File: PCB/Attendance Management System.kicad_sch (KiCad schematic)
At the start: 0 parts

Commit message: Power schematic is ready
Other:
- added sheet MCU (mcu.kicad_sch)
- added sheet Power (power.kicad_sch)
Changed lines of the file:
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@@
 	(generator_version "10.0")
 	(paper "A4")
+	(sheet
+		(at 120.65 83.185)
+		(size 46.99 44.45)
+		(exclude_from_sim no)
+		(in_bom yes)
+		(on_board yes)
+		(dnp no)
+		(fields_autoplaced yes)
+		(stroke
+			(width 0.1524)
+			(type solid)
+		)
+		(fill
+			(color 0 0 0 0)
+		)
+		(property "Sheetname" "MCU"
+			(at 120.65 82.4734 0)
+			(show_name no)
+			(do_not_autoplace no)
+			(effects
+				(font
+					(size 1.27 1.27)
+				)
+				(justify left bottom)
+			)
+		)
+		(property "Sheetfile" "mcu.kicad_sch"
+			(at 120.65 128.2196 0)
+			(show_name no)
+			(do_not_autoplace no)
+			(effects
+				(font
+					(size 1.27 1.27)
+				)
+				(justify left top)
+			)
+		)
+		(instances
+			(project "Attendance Management System"
+				(path "/7913fd27-5946-47b8-84cf-c21ab2f68a0e"
+					(page "3")
+				)
+			)
+		)
+	)
+	(sheet
+		(at 76.835 81.915)
+		(size 20.955 13.335)
+		(exclude_from_sim no)
+		(in_bom yes)
+		(on_board yes)
+		(dnp no)
+		(fields_autoplaced yes)
+		(stroke
+			(width 0.1524)
+			(type solid)
+		)
+		(fill
+			(color 0 0 0 0)
+		)
+		(property "Sheetname" "Power"
+			(at 76.835 81.2034 0)
+			(show_name no)
+			(do_not_autoplace no)
+			(effects
+				(font
+					(size 1.27 1.27)
+				)
+				(justify left bottom)
+			)
+		)
+		(property "Sheetfile" "power.kicad_sch"
+			(at 76.835 95.8346 0)
+			(show_name no)
+			(do_not_autoplace no)
+			(effects
+				(font
+					(size 1.27 1.27)
+				)
+				(justify left top)
+			)
+		)
+		(pin "D-" bidirectional
+			(at 97.79 90.17 0)
+			(effects
+				(font
+					(size 1.27 1.27)
+				)
+				(justify right)
+			)
+		)
+		(pin "D+" bidirectional
+			(at 97.79 86.36 0)
+			(effects
+				(font
+					(size 1.27 1.27)
+				)
+				(justify right)
+			)
+		)
+		(instances
+			(project "Attendance Management System"
+				(path "/7913fd27-5946-47b8-84cf-c21ab2f68a0e"
+					(page "2")
+				)
+			)
+		)
+	)
 	(sheet_instances
 		(path "/"

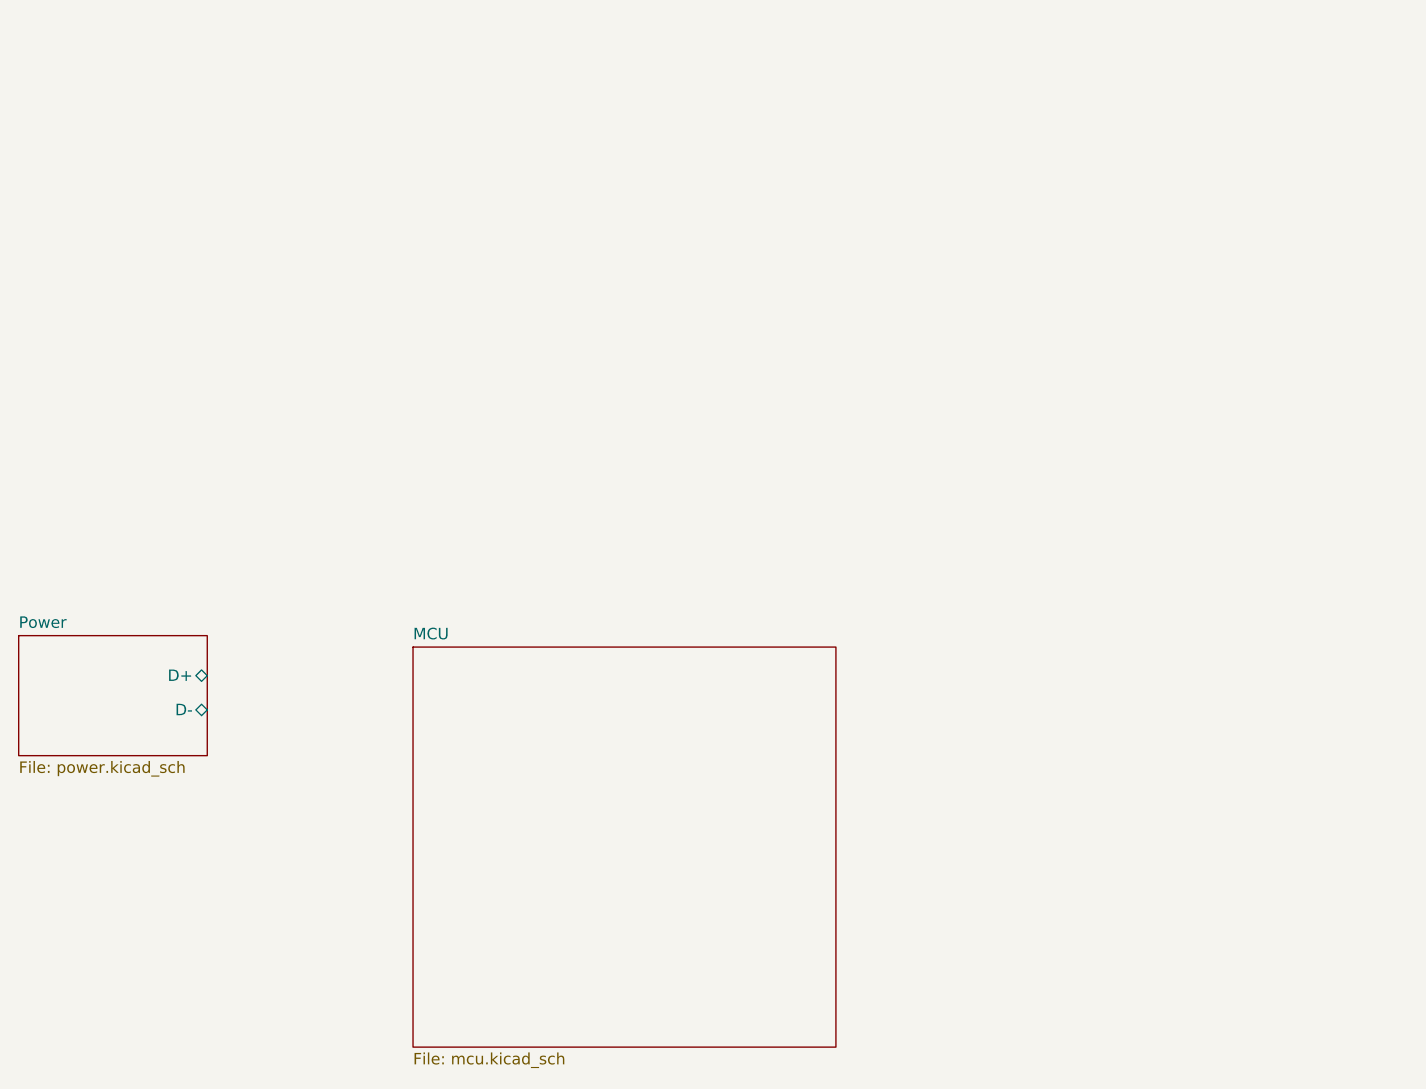
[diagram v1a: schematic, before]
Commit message: RFID sch added
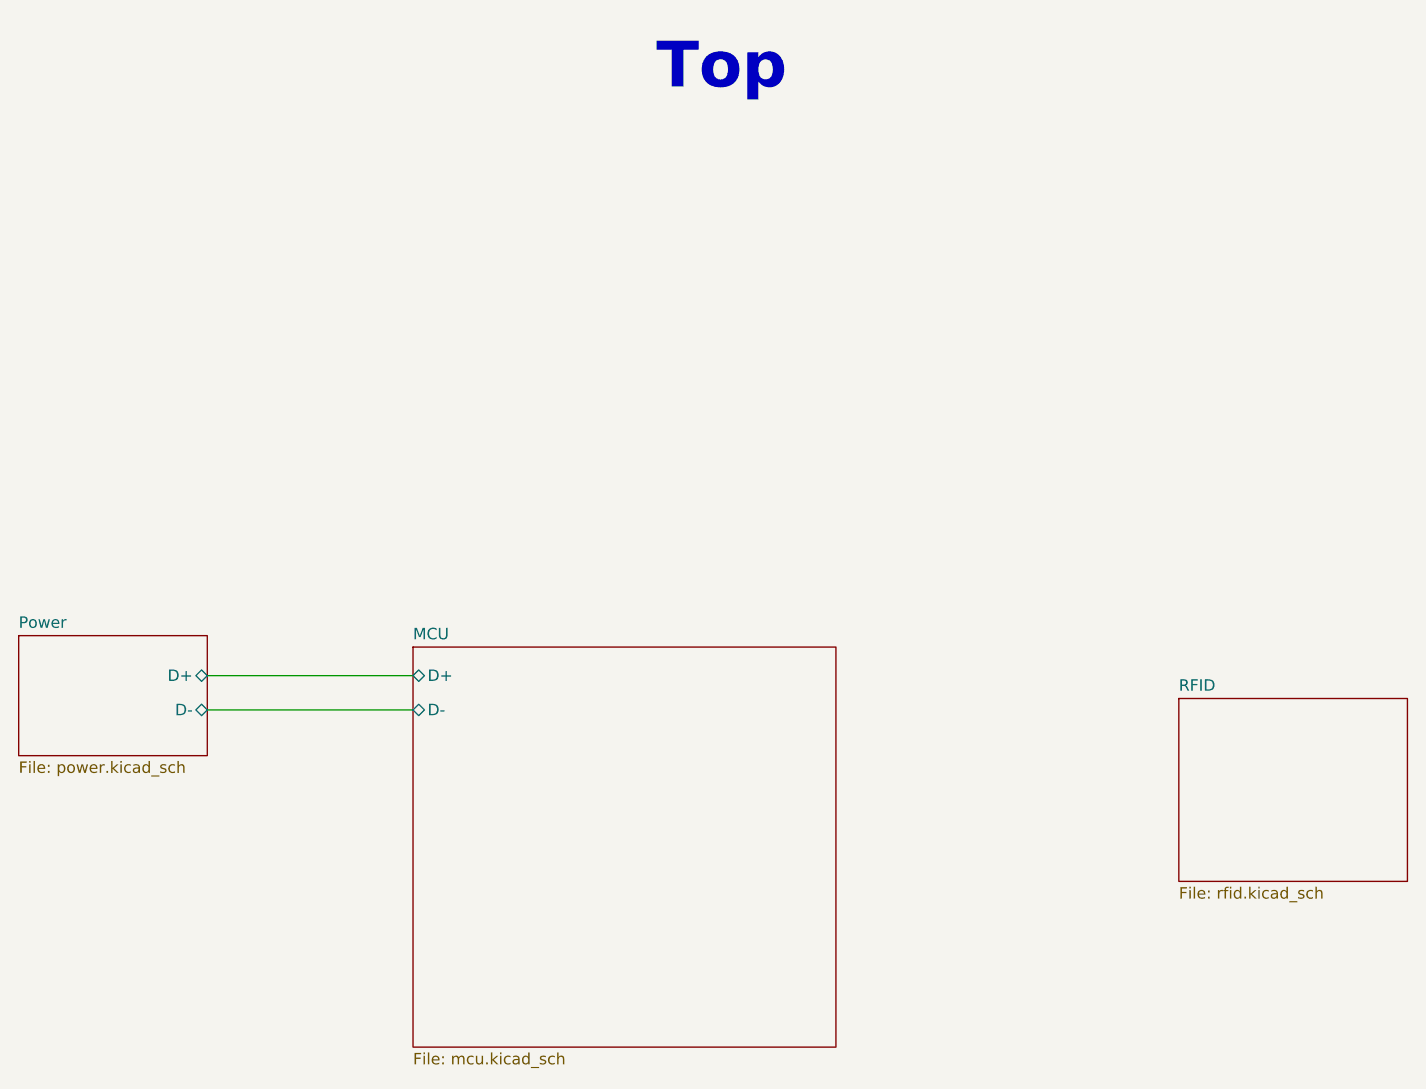
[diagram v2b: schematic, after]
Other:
- added sheet RFID (rfid.kicad_sch)
- sheet MCU ports: added D+, D-; removed none
- note added: "Top"
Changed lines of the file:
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@@
 	(generator_version "10.0")
 	(paper "A4")
+	(text "Top"
+		(exclude_from_sim no)
+		(at 154.94 18.796 0)
+		(effects
+			(font
+				(size 5.08 5.08)
+				(thickness 1.524)
+				(bold yes)
+			)
+		)
+	)
+	(wire
+		(pts
+			(xy 97.79 86.36) (xy 120.65 86.36)
+		)
+		(stroke
+			(width 0)
+			(type default)
+		)
+	)
+	(wire
+		(pts
+			(xy 97.79 90.17) (xy 120.65 90.17)
+		)
+		(stroke
+			(width 0)
+			(type default)
+		)
+	)
 	(sheet
 		(at 120.65 83.185)
@@
 			)
 		)
+		(pin "D+" bidirectional
+			(at 120.65 86.36 180)
+			(effects
+				(font
+					(size 1.27 1.27)
+				)
+				(justify left)
+			)
+		)
+		(pin "D-" bidirectional
+			(at 120.65 90.17 180)
+			(effects
+				(font
+					(size 1.27 1.27)
+				)
+				(justify left)
+			)
+		)
 		(instances
 			(project "Attendance Management System"
@@
 				)
 			)
+		)
+	)
+	(sheet
+		(at 205.74 88.9)
+		(size 25.4 20.32)
+		(exclude_from_sim no)
+		(in_bom yes)
+		(on_board yes)
+		(dnp no)
+		(fields_autoplaced yes)
+		(stroke
+			(width 0.1524)
+			(type solid)
+		)
+		(fill
+			(color 0 0 0 0)
+		)
+		(property "Sheetname" "RFID"
+			(at 205.74 88.1884 0)
+			(show_name no)
+			(do_not_autoplace no)
+			(effects
+				(font
+					(size 1.27 1.27)
+				)
+				(justify left bottom)
+			)
+		)
+		(property "Sheetfile" "rfid.kicad_sch"
+			(at 205.74 109.8046 0)
+			(show_name no)
+			(do_not_autoplace no)
+			(effects
+				(font
+					(size 1.27 1.27)
+				)
+				(justify left top)
+			)
+		)
+		(instances
+			(project "Attendance Management System"
+				(path "/7913fd27-5946-47b8-84cf-c21ab2f68a0e"
+					(page "4")
+				)
+			)
